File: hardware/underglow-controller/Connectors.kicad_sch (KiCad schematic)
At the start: 11 parts, among them J6 DTM1312PA12PBR008, J7 Conn_01x04, J8 Conn_01x05

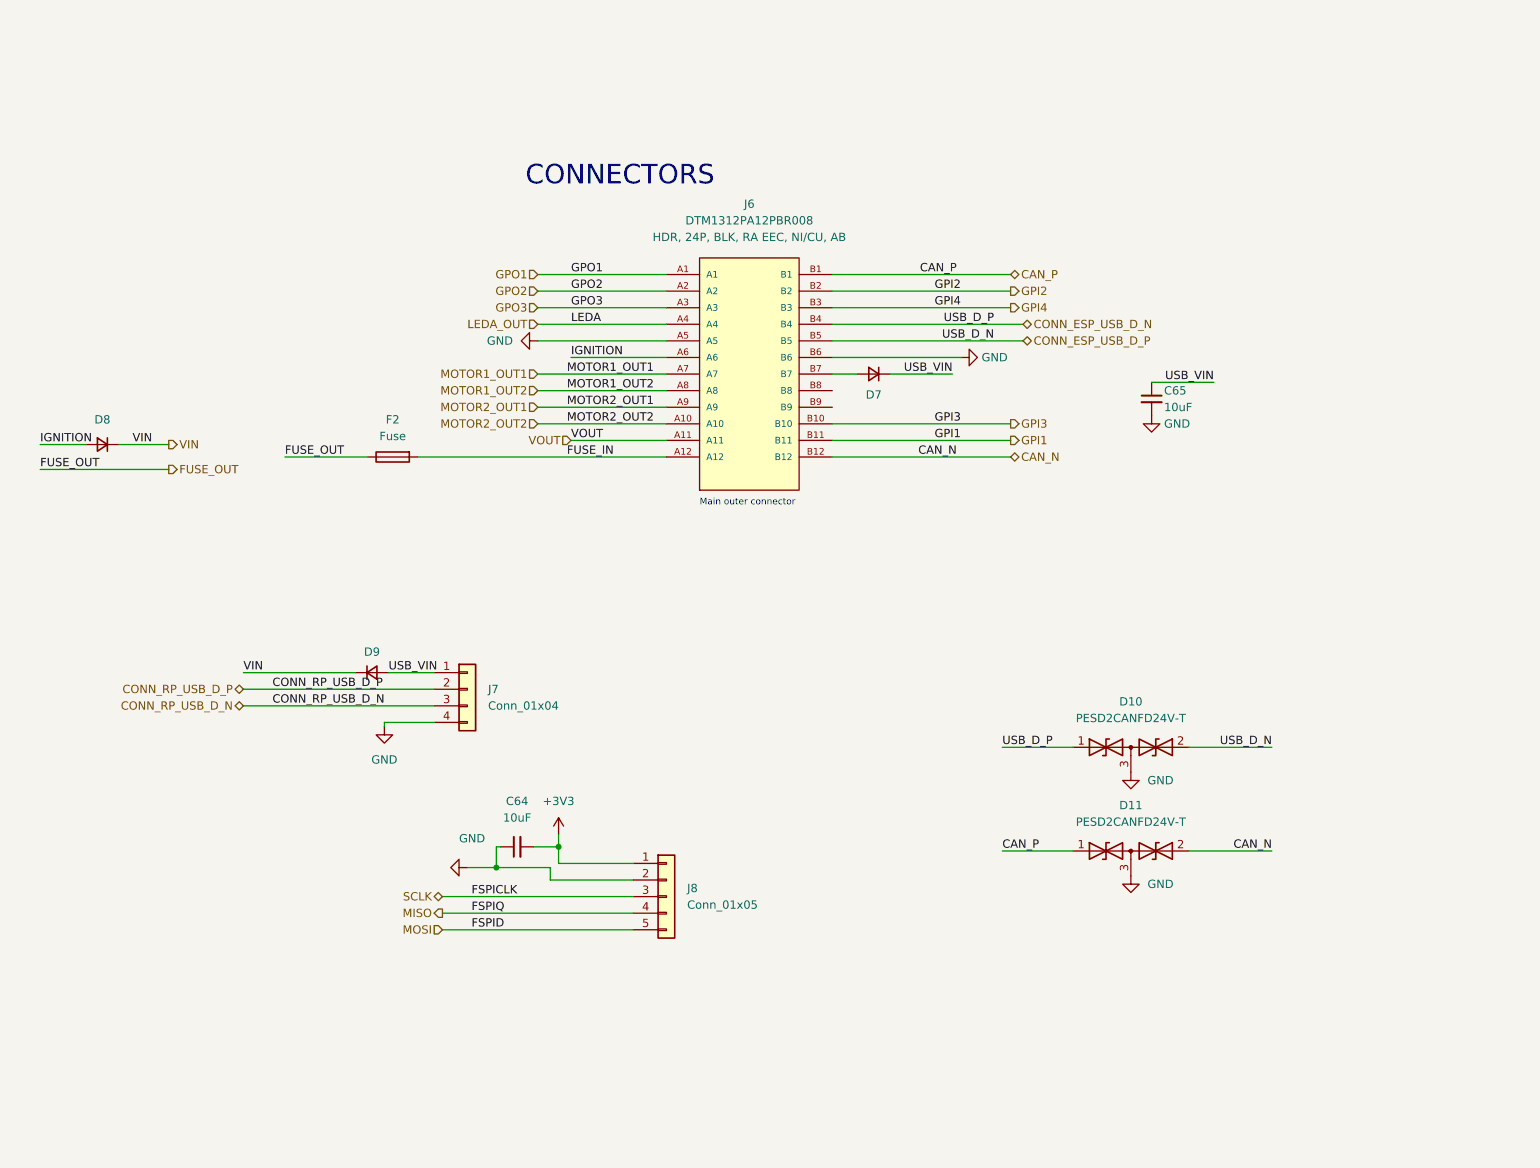
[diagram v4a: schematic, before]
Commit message: replace pmic
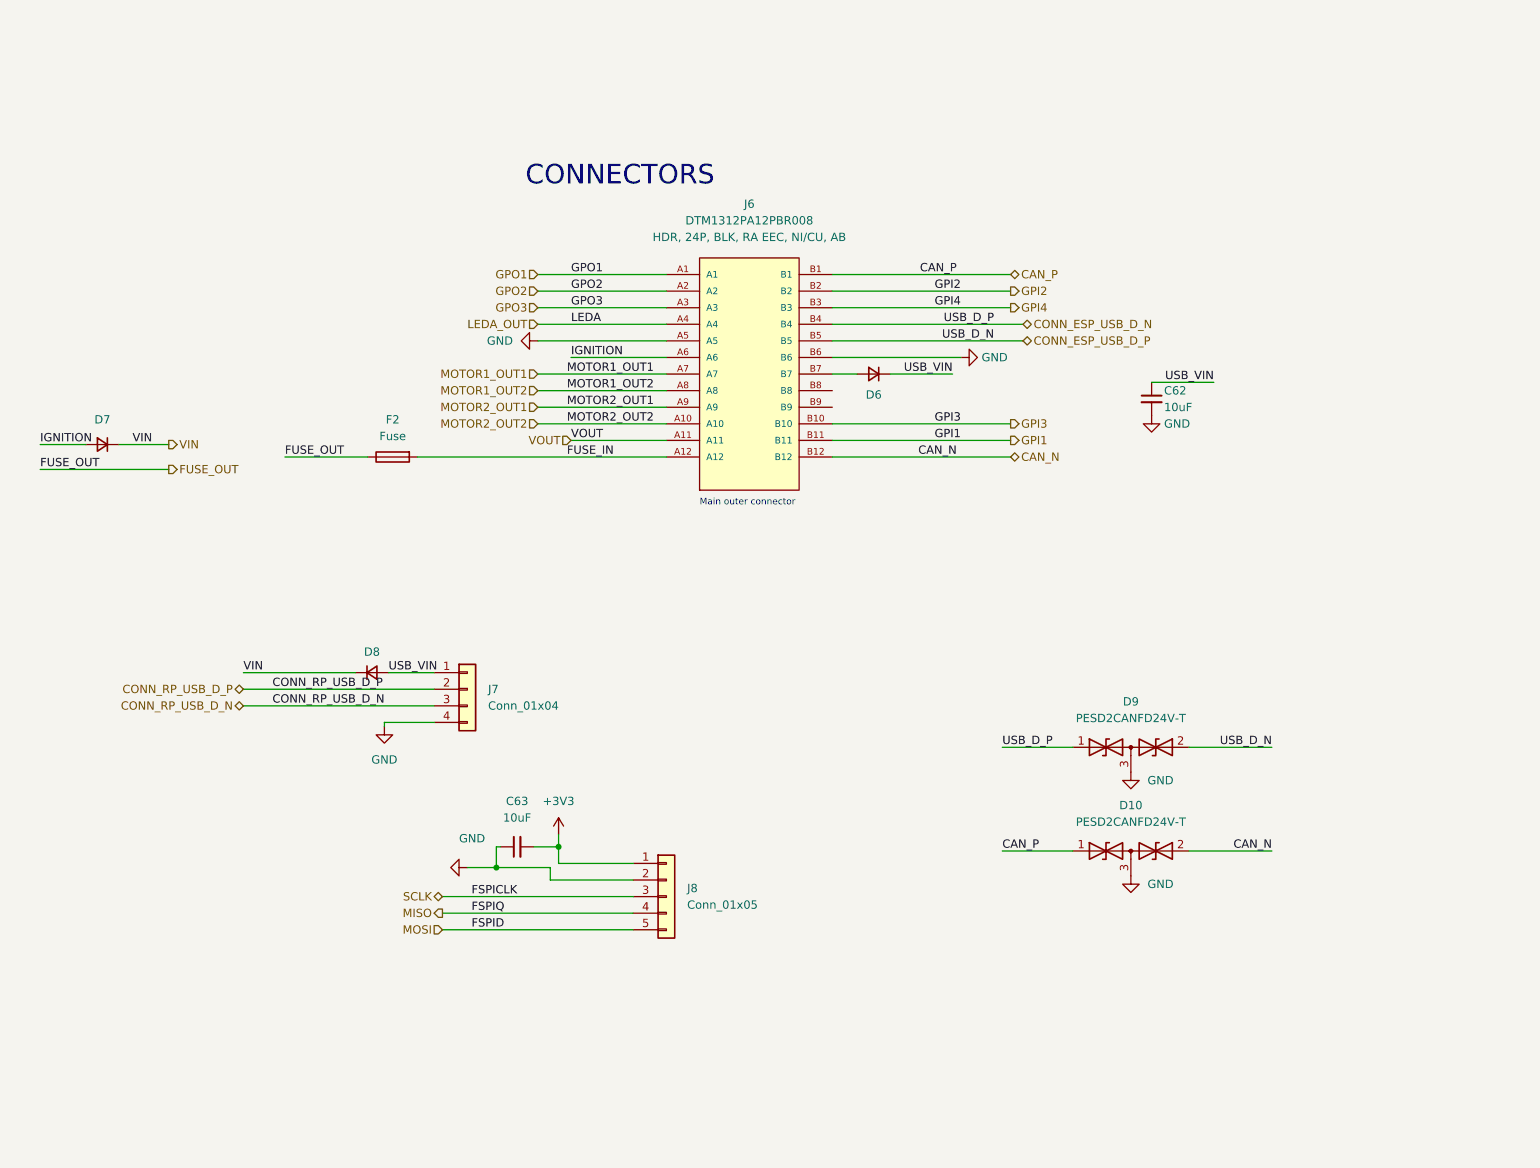
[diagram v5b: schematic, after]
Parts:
- renumbered C65 to C62, C64 to C63, D11 to D10, D7 to D6, D8 to D7, D9 to D8, D10 to D9
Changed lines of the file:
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@@
   (symbol (lib_id "Device:D_TVS_Dual_AAC") (at 187.325 144.78 0) (unit 1)
     (in_bom yes) (on_board yes) (fields_autoplaced)
-    (property "Reference" "D11" (id 0) (at 187.325 137.795 0))
+    (property "Reference" "D10" (id 0) (at 187.325 137.795 0))
     (property "Value" "PESD2CANFD24V-T" (id 1) (at 187.325 140.335 0))
     (property "Footprint" "Package_TO_SOT_SMD:SOT-23" (id 2) (at 183.515 144.78 0)
@@
   (symbol (lib_id "power:GND") (at 187.325 132.715 0) (unit 1)
     (in_bom yes) (on_board yes) (fields_autoplaced)
-    (property "Reference" "#PWR093" (id 0) (at 187.325 139.065 0)
+    (property "Reference" "#PWR095" (id 0) (at 187.325 139.065 0)
       (effects (font (size 1.27 1.27)) hide)
     )
@@
   (symbol (lib_id "Device:D_Small") (at 29.845 82.55 180) (unit 1)
     (in_bom yes) (on_board yes) (fields_autoplaced)
-    (property "Reference" "D8" (id 0) (at 29.845 78.74 0))
+    (property "Reference" "D7" (id 0) (at 29.845 78.74 0))
     (property "Value" "D_Small" (id 1) (at 31.1149 80.01 90)
       (effects (font (size 1.27 1.27)) (justify right) hide)
@@
   (symbol (lib_id "power:GND") (at 187.325 148.59 0) (unit 1)
     (in_bom yes) (on_board yes) (fields_autoplaced)
-    (property "Reference" "#PWR096" (id 0) (at 187.325 154.94 0)
+    (property "Reference" "#PWR098" (id 0) (at 187.325 154.94 0)
       (effects (font (size 1.27 1.27)) hide)
     )
@@
   (symbol (lib_id "Device:C_Small") (at 93.345 144.145 90) (unit 1)
     (in_bom yes) (on_board yes) (fields_autoplaced)
-    (property "Reference" "C64" (id 0) (at 93.3513 137.16 90))
+    (property "Reference" "C63" (id 0) (at 93.3513 137.16 90))
     (property "Value" "10uF" (id 1) (at 93.3513 139.7 90))
     (property "Footprint" "Capacitor_SMD:C_0805_2012Metric" (id 2) (at 93.345 144.145 0)
@@
   (symbol (lib_id "Device:C_Small") (at 190.5 75.565 0) (unit 1)
     (in_bom yes) (on_board yes)
-    (property "Reference" "C65" (id 0) (at 192.405 74.3012 0)
+    (property "Reference" "C62" (id 0) (at 192.405 74.3012 0)
       (effects (font (size 1.27 1.27)) (justify left))
     )
@@
   (symbol (lib_id "Device:D_Small") (at 71.12 117.475 0) (unit 1)
     (in_bom yes) (on_board yes) (fields_autoplaced)
-    (property "Reference" "D9" (id 0) (at 71.12 114.3 0))
+    (property "Reference" "D8" (id 0) (at 71.12 114.3 0))
     (property "Value" "D_Small" (id 1) (at 69.8501 120.015 90)
       (effects (font (size 1.27 1.27)) (justify right) hide)
@@
   (symbol (lib_id "power:GND") (at 85.725 147.32 270) (unit 1)
     (in_bom yes) (on_board yes)
-    (property "Reference" "#PWR095" (id 0) (at 79.375 147.32 0)
+    (property "Reference" "#PWR097" (id 0) (at 79.375 147.32 0)
       (effects (font (size 1.27 1.27)) hide)
     )
@@
   (symbol (lib_id "power:GND") (at 190.5 78.105 0) (unit 1)
     (in_bom yes) (on_board yes) (fields_autoplaced)
-    (property "Reference" "#PWR0101" (id 0) (at 190.5 84.455 0)
+    (property "Reference" "#PWR093" (id 0) (at 190.5 84.455 0)
       (effects (font (size 1.27 1.27)) hide)
     )
@@
   (symbol (lib_id "power:GND") (at 161.29 69.215 90) (unit 1)
     (in_bom yes) (on_board yes) (fields_autoplaced)
-    (property "Reference" "#PWR091" (id 0) (at 167.64 69.215 0)
+    (property "Reference" "#PWR092" (id 0) (at 167.64 69.215 0)
       (effects (font (size 1.27 1.27)) hide)
     )
@@
   (symbol (lib_id "Device:D_TVS_Dual_AAC") (at 187.325 128.905 0) (unit 1)
     (in_bom yes) (on_board yes) (fields_autoplaced)
-    (property "Reference" "D10" (id 0) (at 187.325 121.92 0))
+    (property "Reference" "D9" (id 0) (at 187.325 121.92 0))
     (property "Value" "PESD2CANFD24V-T" (id 1) (at 187.325 124.46 0))
     (property "Footprint" "Package_TO_SOT_SMD:SOT-23" (id 2) (at 183.515 128.905 0)
@@
   (symbol (lib_id "power:GND") (at 73.025 125.73 0) (unit 1)
     (in_bom yes) (on_board yes) (fields_autoplaced)
-    (property "Reference" "#PWR092" (id 0) (at 73.025 132.08 0)
+    (property "Reference" "#PWR094" (id 0) (at 73.025 132.08 0)
       (effects (font (size 1.27 1.27)) hide)
     )
@@
   (symbol (lib_id "Device:D_Small") (at 147.955 71.755 180) (unit 1)
     (in_bom yes) (on_board yes) (fields_autoplaced)
-    (property "Reference" "D7" (id 0) (at 147.955 74.93 0))
+    (property "Reference" "D6" (id 0) (at 147.955 74.93 0))
     (property "Value" "D_Small" (id 1) (at 149.2249 69.215 90)
       (effects (font (size 1.27 1.27)) (justify right) hide)
@@
   (symbol (lib_id "power:GND") (at 96.52 66.675 270) (unit 1)
     (in_bom yes) (on_board yes) (fields_autoplaced)
-    (property "Reference" "#PWR090" (id 0) (at 90.17 66.675 0)
+    (property "Reference" "#PWR091" (id 0) (at 90.17 66.675 0)
       (effects (font (size 1.27 1.27)) hide)
     )
@@
   (symbol (lib_id "power:+3V3") (at 99.695 142.24 0) (unit 1)
     (in_bom yes) (on_board yes) (fields_autoplaced)
-    (property "Reference" "#PWR094" (id 0) (at 99.695 146.05 0)
-      (effects (font (size 1.27 1.27)) hide)
-    )
+    (property "Reference" "#PWR096" (id 0) (at 99.695 146.05 0)
+      (effects (font (size 1.27 1.27)) hide)
+    )

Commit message: iasdf
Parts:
- removed J6: DTM1312PA12PBR008, TE_DTM1312PA12PBR008, symbol ConeCodes:DTM1312PA12PBR008
- added J6: Delphi_Sicma_24, ConeCodes:Delphi_Sicma_24_Black, symbol ConeCodes:Delphi_Sicma_24
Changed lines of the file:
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@@
-    (stroke (width 0) (type default) (color 0 0 0 0))
-  )
-  (wire (pts (xy 96.52 76.835) (xy 116.205 76.835))
     (stroke (width 0) (type default) (color 0 0 0 0))
   )
@@
     (stroke (width 0) (type default) (color 0 0 0 0))
   )
-  (wire (pts (xy 96.52 74.295) (xy 116.205 74.295))
-    (stroke (width 0) (type default) (color 0 0 0 0))
-  )
   (wire (pts (xy 99.695 146.685) (xy 111.125 146.685))
     (stroke (width 0) (type default) (color 0 0 0 0))
@@
     (stroke (width 0) (type default) (color 0 0 0 0))
   )
-  (wire (pts (xy 96.52 71.755) (xy 116.205 71.755))
-    (stroke (width 0) (type default) (color 0 0 0 0))
-  )
   (wire (pts (xy 167.64 128.905) (xy 178.435 128.905))
     (stroke (width 0) (type default) (color 0 0 0 0))
@@
   )
   (wire (pts (xy 141.605 71.755) (xy 145.415 71.755))
-    (stroke (width 0) (type default) (color 0 0 0 0))
-  )
-  (wire (pts (xy 96.52 79.375) (xy 116.205 79.375))
     (stroke (width 0) (type default) (color 0 0 0 0))
   )
@@
     (effects (font (size 1.27 1.27)) (justify right bottom))
   )
-  (label "MOTOR1_OUT2" (at 100.965 74.295 0)
-    (effects (font (size 1.27 1.27)) (justify left bottom))
-  )
   (label "VIN" (at 37.465 82.55 180)
     (effects (font (size 1.27 1.27)) (justify right bottom))
@@
     (effects (font (size 1.27 1.27)) (justify left bottom))
   )
-  (label "VOUT" (at 101.6 81.915 0)
-    (effects (font (size 1.27 1.27)) (justify left bottom))
-  )
   (label "CAN_N" (at 160.655 84.455 180)
     (effects (font (size 1.27 1.27)) (justify right bottom))
@@
     (effects (font (size 1.27 1.27)) (justify left bottom))
   )
-  (label "MOTOR2_OUT2" (at 100.965 79.375 0)
-    (effects (font (size 1.27 1.27)) (justify left bottom))
-  )
-  (label "MOTOR1_OUT1" (at 100.965 71.755 0)
-    (effects (font (size 1.27 1.27)) (justify left bottom))
-  )
-  (label "MOTOR2_OUT1" (at 100.965 76.835 0)
-    (effects (font (size 1.27 1.27)) (justify left bottom))
-  )
   (label "VIN" (at 51.435 117.475 0)
     (effects (font (size 1.27 1.27)) (justify left bottom))
@@
     (effects (font (size 1.27 1.27)) (justify right))
   )
-  (hierarchical_label "MOTOR2_OUT2" (shape input) (at 96.52 79.375 180)
-    (effects (font (size 1.27 1.27)) (justify right))
-  )
   (hierarchical_label "CONN_ESP_USB_D_P" (shape bidirectional) (at 170.815 66.675 0)
     (effects (font (size 1.27 1.27)) (justify left))
@@
     (effects (font (size 1.27 1.27)) (justify right))
   )
-  (hierarchical_label "MOTOR1_OUT2" (shape input) (at 96.52 74.295 180)
-    (effects (font (size 1.27 1.27)) (justify right))
-  )
   (hierarchical_label "GPI2" (shape output) (at 168.91 59.055 0)
     (effects (font (size 1.27 1.27)) (justify left))
@@
   )
   (hierarchical_label "CONN_RP_USB_D_P" (shape bidirectional) (at 51.435 120.015 180)
-    (effects (font (size 1.27 1.27)) (justify right))
-  )
-  (hierarchical_label "MOTOR1_OUT1" (shape input) (at 96.52 71.755 180)
-    (effects (font (size 1.27 1.27)) (justify right))
-  )
-  (hierarchical_label "MOTOR2_OUT1" (shape input) (at 96.52 76.835 180)
     (effects (font (size 1.27 1.27)) (justify right))
   )
@@
     (pin "1")
   )
-  (symbol (lib_id "power:+3V3") (at 99.695 142.24 0) (unit 1)
-    (in_bom yes) (on_board yes) (fields_autoplaced)
-    (property "Reference" "#PWR096" (id 0) (at 99.695 146.05 0)
-      (effects (font (size 1.27 1.27)) hide)
-    )
-    (property "Value" "+3V3" (id 1) (at 99.695 137.16 0))
-    (property "Footprint" "" (id 2) (at 99.695 142.24 0)
-      (effects (font (size 1.27 1.27)) hide)
-    )
-    (property "Datasheet" "" (id 3) (at 99.695 142.24 0)
-      (effects (font (size 1.27 1.27)) hide)
-    )
-    (pin "1")
-  )
-  (symbol (lib_id "ConeCodes:DTM1312PA12PBR008") (at 128.905 69.215 0) (unit 1)
-    (in_bom yes) (on_board yes) (fields_autoplaced)
-    (property "Reference" "J6" (id 0) (at 128.905 45.72 0))
-    (property "Value" "DTM1312PA12PBR008" (id 1) (at 128.905 48.26 0))
-    (property "Footprint" "TE_DTM1312PA12PBR008" (id 2) (at 128.905 69.215 0)
-      (effects (font (size 1.27 1.27)) (justify left bottom) hide)
-    )
-    (property "Datasheet" "https://www.te.com/usa-en/product-DTM1312PA12PBR008.datasheet.pdf" (id 3) (at 128.905 69.215 0)
-      (effects (font (size 1.27 1.27)) (justify left bottom) hide)
-    )
-    (property "MPN" "DTM1312PA12PBR008" (id 7) (at 128.905 69.215 0)
-      (effects (font (size 1.27 1.27)) hide)
-    )
-    (property "Description" "HDR, 24P, BLK, RA EEC, NI/CU, AB" (id 5) (at 128.905 50.8 0))
+  (symbol (lib_id "ConeCodes:Delphi_Sicma_24") (at 233.68 80.01 0) (unit 1)
+    (in_bom yes) (on_board yes) (fields_autoplaced)
+    (property "Reference" "J6" (id 0) (at 233.68 62.23 0))
+    (property "Value" "Delphi_Sicma_24" (id 1) (at 233.68 64.77 0))
+    (property "Footprint" "ConeCodes:Delphi_Sicma_24_Black" (id 2) (at 233.68 63.5 0)
+      (effects (font (size 1.27 1.27)) hide)
+    )
+    (property "Datasheet" "" (id 3) (at 233.68 80.01 0)
+      (effects (font (size 1.27 1.27)) hide)
+    )
     (pin "A1")
-    (pin "A10")
-    (pin "A11")
-    (pin "A12")
     (pin "A2")
     (pin "A3")
@@
     (pin "A7")
     (pin "A8")
-    (pin "A9")
     (pin "B1")
-    (pin "B10")
-    (pin "B11")
-    (pin "B12")
     (pin "B2")
     (pin "B3")
@@
     (pin "B7")
     (pin "B8")
-    (pin "B9")
+    (pin "C1")
+    (pin "C2")
+    (pin "C3")
+    (pin "C4")
+    (pin "C5")
+    (pin "C6")
+    (pin "C7")
+    (pin "C8")
+  )
+  (symbol (lib_id "power:+3V3") (at 99.695 142.24 0) (unit 1)
+    (in_bom yes) (on_board yes) (fields_autoplaced)
+    (property "Reference" "#PWR096" (id 0) (at 99.695 146.05 0)
+      (effects (font (size 1.27 1.27)) hide)
+    )
+    (property "Value" "+3V3" (id 1) (at 99.695 137.16 0))
+    (property "Footprint" "" (id 2) (at 99.695 142.24 0)
+      (effects (font (size 1.27 1.27)) hide)
+    )
+    (property "Datasheet" "" (id 3) (at 99.695 142.24 0)
+      (effects (font (size 1.27 1.27)) hide)
+    )
+    (pin "1")
   )
   (symbol (lib_id "Connector_Generic:Conn_01x05") (at 116.205 151.765 0) (unit 1)

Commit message: schematic rework progress
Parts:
- removed D6, D7, D8: D_Small, Diode_SMD:D_SOD-123F, symbol Device:D_Small
- removed F2: Fuse, ConeCodes:Keystone-3587-10TR, symbol Device:Fuse
- removed J7: Conn_01x04, Connector_PinHeader_1.27mm:PinHeader_1x04_P1.27mm_Vertical, symbol Connector_Generic:Conn_01x04
- renumbered C62 to C60, C63 to C61, D9 to D8, D10 to D9, J6 to J5, J8 to J7
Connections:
- net CAN_N is gone; now on net CAN_L: D9.2 (A2)
- net CAN_P is gone; now on net CAN_H: D9.1 (A1)
- net CONN_ESP_USB_D_N is gone; now on net USB_D_P: D8.1 (A1)
- net CONN_ESP_USB_D_P is gone; now on net USB_D_N: D8.2 (A2)
- net USB_VIN is gone; now on net USB_VBUS: C60.1
- net GND: now also J5.A8, J5.B2; no longer C60.2
- net IGNITION_IN: now reaches J5.A1
- net RGB1_R: now reaches J5.A2
- net RGB1_G: now reaches J5.A3
- net RGB1_B: now reaches J5.A4
- net RGB2_R: now reaches J5.A5
- net RGB2_G: now reaches J5.A6
- net RGB2_B: now reaches J5.A7
- net VBAT: now reaches J5.B1
- net CAN_H: now reaches J5.B3
- net CAN_L: now reaches J5.B4
- net USB_GND: now reaches J5.B5
- net USB_GND: now also C60.2
- net USB_D_P: now reaches J5.B6
- net USB_D_N: now reaches J5.B7
- net USB_VBUS: now reaches J5.B8
- net RGB2_12V: now reaches J5.C1
- net DI_1: now reaches J5.C2
- net DI_2: now reaches J5.C3
- net DI_3: now reaches J5.C4
- net DI_4: now reaches J5.C5
- net PIXEL_2: now reaches J5.C6
- net PIXEL_1: now reaches J5.C7
- net RGB1_12V: now reaches J5.C8
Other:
- note removed: "Main outer connector"
- moved on the sheet: C60, C61, D8, D9, J5, J7

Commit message: schematic almost done
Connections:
- net IGNITION_IN renamed IGNITION
- net VBAT renamed VBATT
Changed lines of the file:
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@@
     (stroke (width 0) (type default) (color 255 255 255 1))
+  )
+  (wire (pts (xy 32.385 53.34) (xy 45.72 53.34))
+    (stroke (width 0) (type default) (color 255 153 0 1))
   )
   (wire (pts (xy 64.77 35.56) (xy 88.9 35.56))
@@
     (stroke (width 0) (type default) (color 132 0 0 1))
   )
-  (wire (pts (xy 32.385 53.34) (xy 45.72 53.34))
-    (stroke (width 0) (type default) (color 255 153 0 1))
-  )
   (wire (pts (xy 32.385 40.64) (xy 52.07 40.64))
     (stroke (width 0) (type default) (color 0 255 0 1))
@@
     (effects (font (size 1.27 1.27)) (justify right bottom))
   )
-  (label "IGNITION_IN" (at 32.385 53.34 0)
+  (label "IGNITION" (at 32.385 53.34 0)
     (effects (font (size 1.27 1.27)) (justify left bottom))
   )
@@
     (effects (font (size 1.27 1.27)) (justify right))
   )
-  (hierarchical_label "USB_GND" (shape passive) (at 107.95 71.755 0)
-    (effects (font (size 1.27 1.27)) (justify left))
-  )
-  (hierarchical_label "VBAT" (shape input) (at 32.385 62.23 180)
+  (hierarchical_label "USB_GND" (shape input) (at 107.95 71.755 0)
+    (effects (font (size 1.27 1.27)) (justify left))
+  )
+  (hierarchical_label "VBATT" (shape input) (at 32.385 62.23 180)
     (effects (font (size 1.27 1.27)) (justify right))
   )
@@
     (effects (font (size 1.27 1.27)) (justify left))
   )
-  (hierarchical_label "IGNITION_IN" (shape input) (at 32.385 53.34 180)
-    (effects (font (size 1.27 1.27)) (justify right))
-  )
+  (hierarchical_label "IGNITION" (shape output) (at 32.385 53.34 180)
+    (effects (font (size 1.27 1.27)) (justify right))
+  )
